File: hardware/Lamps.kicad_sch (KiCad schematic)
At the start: 3 parts

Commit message: 2/static version
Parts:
- removed C501: 100uF 10V, Capacitor_THT:CP_Radial_D6.3mm_P2.50mm, symbol Device:C_Polarized
- removed D501: ES1J, Diode_SMD:D_SMA_Handsoldering, symbol Device:D
- removed R501: 330R, Resistor_SMD:R_0603_1608Metric, symbol Device:R
- added C401: 100uF 10V, Capacitor_THT:CP_Radial_D6.3mm_P2.50mm, symbol Device:C_Polarized
- added D401: ES1J, Diode_SMD:D_SMA, symbol Device:D
- added N401, N402, N403, N404: INS-1, mynixies:mynixies-INS-1, symbol mynixies:INS-1
- added Q401: MPSA42, Package_TO_SOT_THT:TO-92_Inline, symbol Transistor_BJT:MPSA42
- added R401, R402, R405, R407: 330K, Resistor_SMD:R_1206_3216Metric, symbol Device:R
- added R403: 10K, Resistor_SMD:R_0603_1608Metric, symbol Device:R
- added R404: 47K, Resistor_SMD:R_0603_1608Metric, symbol Device:R
- added R406: 330R, Resistor_SMD:R_0603_1608Metric, symbol Device:R
- added U401: 74HC595, Package_SO:TSSOP-16_4.4x5mm_P0.65mm, symbol 74xx:74HC595
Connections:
- net +5V: now also C401.2, D401.2 (A)
- net GND: now also C401.1, Q401.1 (E), R404.1, U401.13 (~{OE}), U401.8 (GND)
- new net: Q401.3 (C), R401.1, R402.1, R405.1, R407.1
- new net: N401.P$1 (C), R401.2
- new net: Q401.2 (B), R403.2, R404.2
- new net: N403.P$1 (C), R405.2
- new net: N404.P$1 (C), R407.2
- new net: N402.P$1 (C), R402.2
- new net +170V: N401.P$2 (A), N402.P$2 (A), N403.P$2 (A), N404.P$2 (A)
- new net +3V3: U401.10 (~{SRCLR}), U401.16 (VCC)
- new net COLONS: R403.1
- new net CS: U401.12 (RCLK)
- new net FIRST_SK6812MINI_VCC: D401.1 (K)
- new net SCK: U401.11 (SRCLK)
- new net SER: U401.14 (SER)
- new net SK6812MINI_DATA: R406.1
- new net ThreeDigits1/DIGIT_A: U401.15 (QA)
- new net ThreeDigits1/DIGIT_B: U401.1 (QB)
- new net ThreeDigits1/DIGIT_C: U401.2 (QC)
- new net ThreeDigits1/DIGIT_D: U401.3 (QD)
- new net ThreeDigits1/SK6812MINI_IN: R406.2
- new net ThreeDigits2/DIGIT_A: U401.4 (QE)
- new net ThreeDigits2/DIGIT_B: U401.5 (QF)
- new net ThreeDigits2/DIGIT_C: U401.6 (QG)
- new net ThreeDigits2/DIGIT_D: U401.7 (QH)
- no-connect marks 1 -> 2
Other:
- removed sheet Dots
- removed sheet TwoDigits1
- removed sheet TwoDigits2
- removed sheet TwoDigits3
- added sheet HighSideSwitch1 (HighSideSwitch.kicad_sch)
- added sheet HighSideSwitch2 (HighSideSwitch.kicad_sch)
- added sheet HighSideSwitch3 (HighSideSwitch.kicad_sch)
- added sheet ThreeDigits1 (ThreeDigits.kicad_sch)
- added sheet ThreeDigits2 (ThreeDigits.kicad_sch)

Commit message: Finalize schematics
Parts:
- N401, N402, N403, N404: footprint mynixies:mynixies-INS-1 -> NosLib:INS-1
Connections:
- net FIRST_SK6812MINI_VCC renamed ThreeDigits1/FIRST_SK6812MINI_VCC
- no-connect marks 2 -> 1
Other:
- moved on the sheet: C401, D401
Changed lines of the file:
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@@
 	)
 	(junction
-		(at 40.64 88.9)
+		(at 82.55 87.63)
 		(diameter 0)
 		(color 0 0 0 0)
@@
 	)
 	(junction
+		(at 96.52 87.63)
+		(diameter 0)
+		(color 0 0 0 0)
+	)
+	(junction
 		(at 128.27 81.28)
 		(diameter 0)
@@
 	)
 	(no_connect
-		(at 68.58 152.4)
-	)
-	(no_connect
 		(at 147.32 175.26)
 	)
@@
 	(wire
 		(pts
-			(xy 48.26 88.9) (xy 53.34 88.9)
+			(xy 90.17 87.63) (xy 96.52 87.63)
 		)
 		(stroke
@@
 	(wire
 		(pts
-			(xy 34.29 88.9) (xy 40.64 88.9)
+			(xy 76.2 87.63) (xy 82.55 87.63)
 		)
 		(stroke
@@
 	(wire
 		(pts
-			(xy 68.58 152.4) (xy 67.31 152.4)
-		)
-		(stroke
-			(width 0)
-			(type default)
-		)
-	)
-	(wire
-		(pts
 			(xy 128.27 81.28) (xy 152.4 81.28)
 		)
@@
 	(wire
 		(pts
+			(xy 96.52 87.63) (xy 121.92 87.63)
+		)
+		(stroke
+			(width 0)
+			(type default)
+		)
+	)
+	(wire
+		(pts
 			(xy 67.31 132.08) (xy 87.63 132.08)
 		)
@@
 		)
 	)
-	(label "FIRST_SK6812MINI_VCC"
-		(at 121.92 87.63 180)
-		(effects
-			(font
-				(size 1.27 1.27)
-			)
-			(justify right bottom)
-		)
-	)
-	(label "FIRST_SK6812MINI_VCC"
-		(at 53.34 88.9 0)
-		(effects
-			(font
-				(size 1.27 1.27)
-			)
-			(justify left bottom)
-		)
-	)
 	(hierarchical_label "+3V3"
 		(shape input)
@@
 	(hierarchical_label "+5V"
 		(shape input)
-		(at 34.29 88.9 180)
+		(at 76.2 87.63 180)
 		(effects
 			(font
@@
 	)
 	(symbol
+		(lib_id "power:PWR_FLAG")
+		(at 96.52 87.63 0)
+		(unit 1)
+		(exclude_from_sim no)
+		(in_bom yes)
+		(on_board yes)
+		(dnp no)
+		(fields_autoplaced yes)
+		(property "Reference" "#FLG0401"
+			(at 96.52 85.725 0)
+			(effects
+				(font
+					(size 1.27 1.27)
+				)
+				(hide yes)
+			)
+		)
+		(property "Value" "PWR_FLAG"
+			(at 96.52 82.55 0)
+			(effects
+				(font
+					(size 1.27 1.27)
+				)
+			)
+		)
+		(property "Footprint" ""
+			(at 96.52 87.63 0)
+			(effects
+				(font
+					(size 1.27 1.27)
+				)
+				(hide yes)
+			)
+		)
+		(property "Datasheet" "~"
+			(at 96.52 87.63 0)
+			(effects
+				(font
+					(size 1.27 1.27)
+				)
+				(hide yes)
+			)
+		)
+		(property "Description" "Special symbol for telling ERC where power comes from"
+			(at 96.52 87.63 0)
+			(effects
+				(font
+					(size 1.27 1.27)
+				)
+				(hide yes)
+			)
+		)
+		(pin "1"
+		)
+		(instances
+			(project "NosClock"
+				(path "/5a46aee9-b968-477e-a4a1-4edba06163a3/cbfce168-24b0-4ff9-a45f-71f9f499ca5c"
+					(reference "#FLG0401")
+					(unit 1)
+				)
+			)
+		)
+	)
+	(symbol
 		(lib_id "Device:R")
 		(at 240.03 40.64 90)
@@
 	(symbol
 		(lib_id "Device:D")
-		(at 44.45 88.9 180)
+		(at 86.36 87.63 180)
 		(unit 1)
 		(exclude_from_sim no)
@@
 		(fields_autoplaced yes)
 		(property "Reference" "D401"
-			(at 44.45 82.55 0)
+			(at 86.36 81.28 0)
 			(effects
 				(font
@@
 		)
 		(property "Value" "ES1J"
-			(at 44.45 85.09 0)
+			(at 86.36 83.82 0)
 			(effects
 				(font
@@
 		)
 		(property "Footprint" "Diode_SMD:D_SMA"
-			(at 44.45 88.9 0)
+			(at 86.36 87.63 0)
 			(effects
 				(font
@@
 		)
 		(property "Datasheet" "~"
-			(at 44.45 88.9 0)
+			(at 86.36 87.63 0)
 			(effects
 				(font
@@
 		)
 		(property "Description" "Diode"
-			(at 44.45 88.9 0)
+			(at 86.36 87.63 0)
 			(effects
 				(font
@@
 		)
 		(property "Sim.Device" "D"
-			(at 44.45 88.9 0)
+			(at 86.36 87.63 0)
 			(effects
 				(font
@@
 		)
 		(property "Sim.Pins" "1=K 2=A"
-			(at 44.45 88.9 0)
+			(at 86.36 87.63 0)
 			(effects
 				(font
@@
 		)
 		(property "Availability" ""
-			(at 44.45 88.9 0)
+			(at 86.36 87.63 0)
 			(effects
 				(font
@@
 		)
 		(property "Check_prices" ""
-			(at 44.45 88.9 0)
+			(at 86.36 87.63 0)
 			(effects
 				(font
@@
 		)
 		(property "Description_1" ""
-			(at 44.45 88.9 0)
+			(at 86.36 87.63 0)
 			(effects
 				(font
@@
 		)
 		(property "MF" ""
-			(at 44.45 88.9 0)
+			(at 86.36 87.63 0)
 			(effects
 				(font
@@
 		)
 		(property "MP" ""
-			(at 44.45 88.9 0)
+			(at 86.36 87.63 0)
 			(effects
 				(font
@@
 		)
 		(property "PARTNO" ""
-			(at 44.45 88.9 0)
+			(at 86.36 87.63 0)
 			(effects
 				(font
@@
 		)
 		(property "Package" ""
-			(at 44.45 88.9 0)
+			(at 86.36 87.63 0)
 			(effects
 				(font
@@
 		)
 		(property "Price" ""
-			(at 44.45 88.9 0)
+			(at 86.36 87.63 0)
 			(effects
 				(font
@@
 		)
 		(property "SnapEDA_Link" ""
-			(at 44.45 88.9 0)
+			(at 86.36 87.63 0)
 			(effects
 				(font
@@
 			)
 		)
-		(property "Footprint" "mynixies:mynixies-INS-1"
+		(property "Footprint" "NosLib:INS-1"
 			(at 252.222 101.6 0)
 			(effects
@@
 	(symbol
 		(lib_id "power:GND")
-		(at 40.64 96.52 0)
+		(at 82.55 95.25 0)
 		(unit 1)
 		(exclude_from_sim no)
@@
 		(fields_autoplaced yes)
 		(property "Reference" "#PWR0401"
-			(at 40.64 102.87 0)
+			(at 82.55 101.6 0)
 			(effects
 				(font
@@
 		)
 		(property "Value" "GND"
-			(at 40.64 101.6 0)
+			(at 82.55 100.33 0)
 			(effects
 				(font
@@
 		)
 		(property "Footprint" ""
-			(at 40.64 96.52 0)
+			(at 82.55 95.25 0)
 			(effects
 				(font
@@
 		)
 		(property "Datasheet" ""
-			(at 40.64 96.52 0)
+			(at 82.55 95.25 0)
 			(effects
 				(font
@@
 		)
 		(property "Description" "Power symbol creates a global label with name \"GND\" , ground"
-			(at 40.64 96.52 0)
+			(at 82.55 95.25 0)
 			(effects
 				(font
@@
 	(symbol
 		(lib_id "Device:C_Polarized")
-		(at 40.64 92.71 180)
+		(at 82.55 91.44 180)
 		(unit 1)
 		(exclude_from_sim no)
@@
 		(fields_autoplaced yes)
 		(property "Reference" "C401"
-			(at 44.45 92.3289 0)
+			(at 86.36 91.0589 0)
 			(effects
 				(font
@@
 		)
 		(property "Value" "100uF 10V"
-			(at 44.45 94.8689 0)
+			(at 86.36 93.5989 0)
 			(effects
 				(font
@@
 		)
 		(property "Footprint" "Capacitor_THT:CP_Radial_D6.3mm_P2.50mm"
-			(at 39.6748 88.9 0)
+			(at 81.5848 87.63 0)
 			(effects
 				(font
@@
 		)
 		(property "Datasheet" "~"
-			(at 40.64 92.71 0)
+			(at 82.55 91.44 0)
 			(effects
 				(font
@@
 		)
 		(property "Description" "Polarized capacitor"
-			(at 40.64 92.71 0)
+			(at 82.55 91.44 0)
 			(effects
 				(font
@@
 			)
 		)
-		(property "Footprint" "mynixies:mynixies-INS-1"
+		(property "Footprint" "NosLib:INS-1"
 			(at 252.222 128.27 0)
 			(effects
@@
 			)
 		)
-		(property "Footprint" "mynixies:mynixies-INS-1"
+		(property "Footprint" "NosLib:INS-1"
 			(at 252.222 36.83 0)
 			(effects
@@
 			)
 		)
-		(property "Footprint" "mynixies:mynixies-INS-1"
+		(property "Footprint" "NosLib:INS-1"
 			(at 252.222 63.5 0)
 			(effects

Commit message: Fixes
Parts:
- removed Q401: MPSA42, Package_TO_SOT_THT:TO-92_Inline, symbol Transistor_BJT:MPSA42
- added Q402: MMBTA42, Package_TO_SOT_SMD:SOT-23, symbol Transistor_BJT:MMBTA42
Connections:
- net GND: now also Q402.2 (E)
- net at R401.1, R402.1, R405.1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: now also Q402.3 (C)
- net at R403.2, R404.2: now also Q402.1 (B)
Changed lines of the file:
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@@
-	)
-	(symbol
-		(lib_id "Transistor_BJT:MPSA42")
-		(at 214.63 95.25 0)
-		(unit 1)
-		(exclude_from_sim no)
-		(in_bom yes)
-		(on_board yes)
-		(dnp no)
-		(fields_autoplaced yes)
-		(property "Reference" "Q401"
-			(at 219.71 93.9799 0)
-			(effects
-				(font
-					(size 1.27 1.27)
-				)
-				(justify left)
-			)
-		)
-		(property "Value" "MPSA42"
-			(at 219.71 96.5199 0)
-			(effects
-				(font
-					(size 1.27 1.27)
-				)
-				(justify left)
-			)
-		)
-		(property "Footprint" "Package_TO_SOT_THT:TO-92_Inline"
-			(at 219.71 97.155 0)
-			(effects
-				(font
-					(size 1.27 1.27)
-					(italic yes)
-				)
-				(justify left)
-				(hide yes)
-			)
-		)
-		(property "Datasheet" "http://www.onsemi.com/pub_link/Collateral/MPSA42-D.PDF"
-			(at 214.63 95.25 0)
-			(effects
-				(font
-					(size 1.27 1.27)
-				)
-				(justify left)
-				(hide yes)
-			)
-		)
-		(property "Description" "0.5A Ic, 300V Vce, NPN High Voltage Transistor, TO-92"
-			(at 214.63 95.25 0)
-			(effects
-				(font
-					(size 1.27 1.27)
-				)
-				(hide yes)
-			)
-		)
-		(pin "2"
-		)
-		(pin "3"
-		)
-		(pin "1"
-		)
-		(instances
-			(project "NosClock"
-				(path "/5a46aee9-b968-477e-a4a1-4edba06163a3/cbfce168-24b0-4ff9-a45f-71f9f499ca5c"
-					(reference "Q401")
-					(unit 1)
-				)
-			)
-		)
 	)
 	(symbol
@@
 					(unit 1)
 				)
+			)
+		)
+	)
+	(symbol
+		(lib_id "Transistor_BJT:MMBTA42")
+		(at 214.63 95.25 0)
+		(unit 1)
+		(exclude_from_sim no)
+		(in_bom yes)
+		(on_board yes)
+		(dnp no)
+		(fields_autoplaced yes)
+		(property "Reference" "Q402"
+			(at 219.71 93.9799 0)
+			(effects
+				(font
+					(size 1.27 1.27)
+				)
+				(justify left)
+			)
+		)
+		(property "Value" "MMBTA42"
+			(at 219.71 96.5199 0)
+			(effects
+				(font
+					(size 1.27 1.27)
+				)
+				(justify left)
+			)
+		)
+		(property "Footprint" "Package_TO_SOT_SMD:SOT-23"
+			(at 219.71 97.155 0)
+			(effects
+				(font
+					(size 1.27 1.27)
+					(italic yes)
+				)
+				(justify left)
+				(hide yes)
+			)
+		)
+		(property "Datasheet" "https://www.onsemi.com/pub/Collateral/MMBTA42LT1-D.PDF"
+			(at 214.63 95.25 0)
+			(effects
+				(font
+					(size 1.27 1.27)
+				)
+				(justify left)
+				(hide yes)
+			)
+		)
+		(property "Description" "0.5A Ic, 300V Vce, NPN High Voltage Transistor, SOT-23"
+			(at 214.63 95.25 0)
+			(effects
+				(font
+					(size 1.27 1.27)
+				)
+				(hide yes)
+			)
+		)
+		(pin "3"
+		)
+		(pin "1"
+		)
+		(pin "2"
+		)
+		(instances
+			(project "NosClock"
+				(path "/5a46aee9-b968-477e-a4a1-4edba06163a3/cbfce168-24b0-4ff9-a45f-71f9f499ca5c"
+					(reference "Q402")
+					(unit 1)
+				)

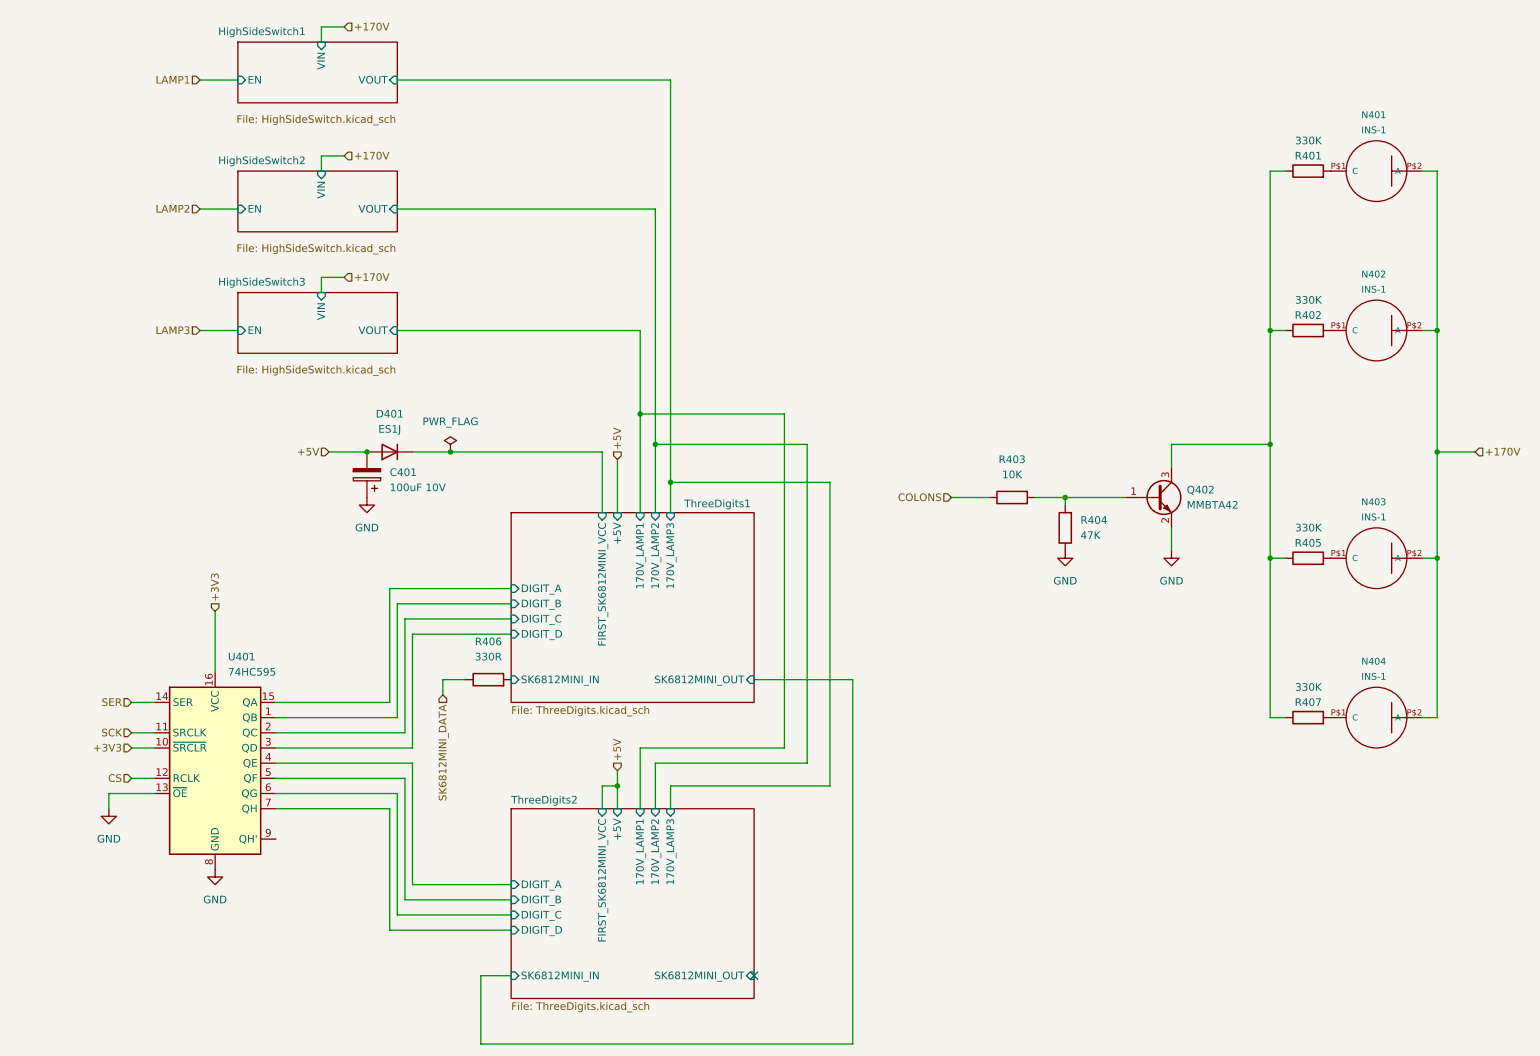
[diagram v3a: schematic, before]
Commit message: Lamps tracing
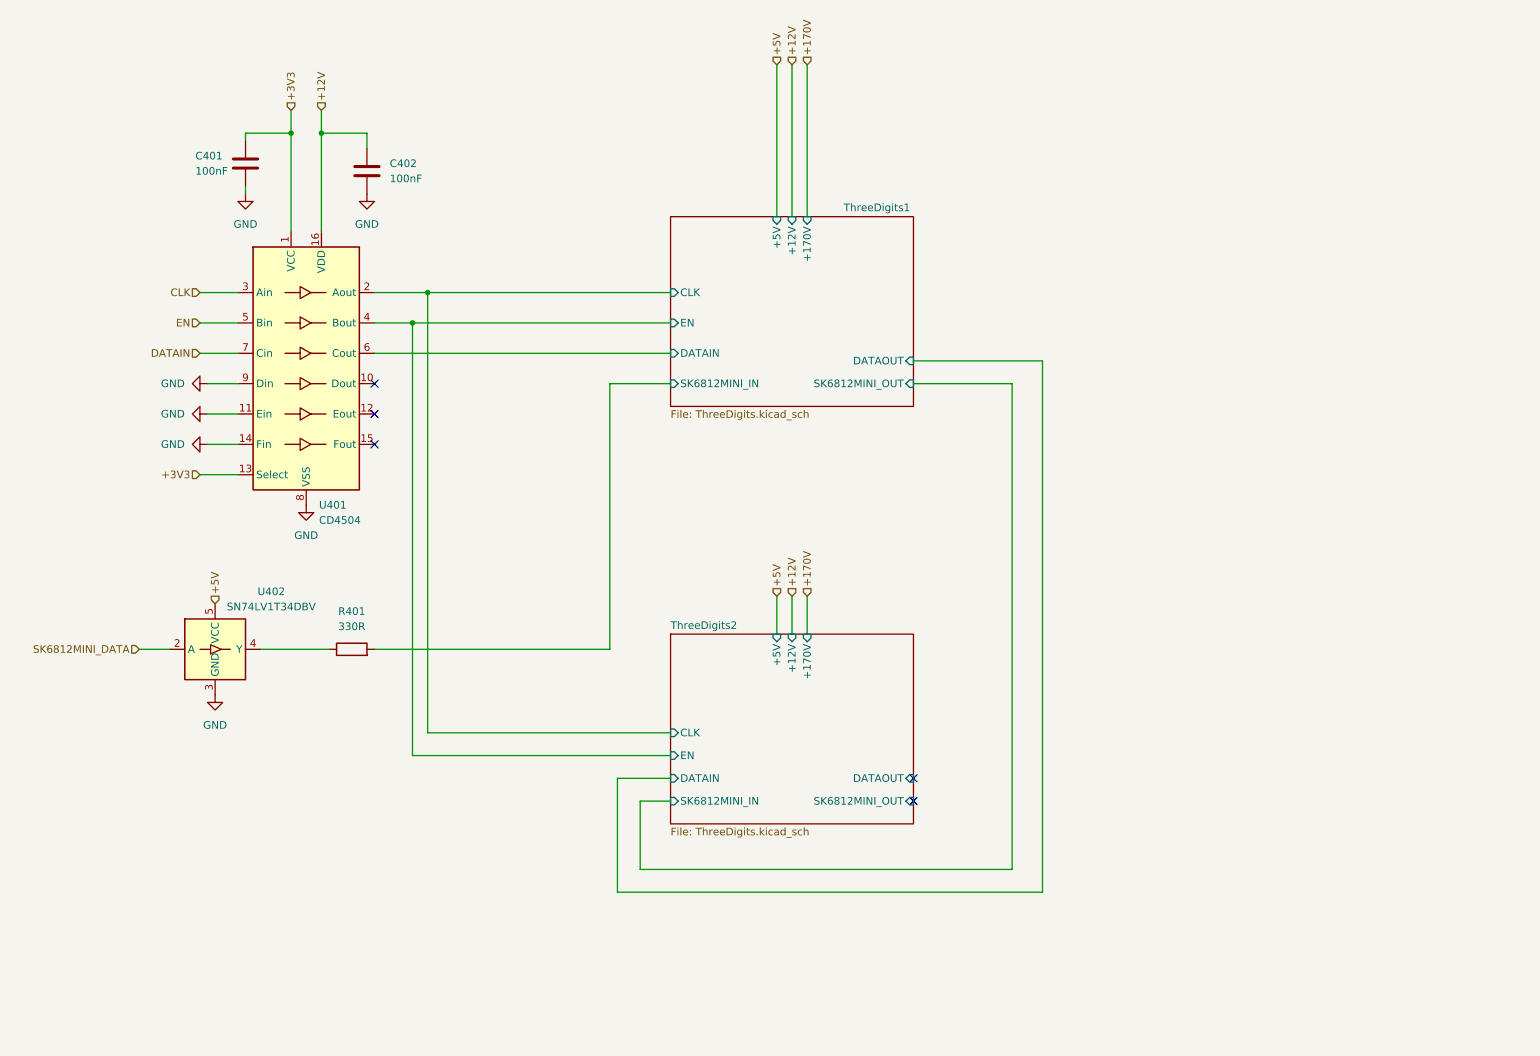
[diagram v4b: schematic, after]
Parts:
- removed C401: 100uF 10V, Capacitor_THT:CP_Radial_D6.3mm_P2.50mm, symbol Device:C_Polarized
- removed D401: ES1J, Diode_SMD:D_SMA, symbol Device:D
- removed N401, N402, N403, N404: INS-1, NosLib:INS-1, symbol mynixies:INS-1
- removed Q402: MMBTA42, Package_TO_SOT_SMD:SOT-23, symbol Transistor_BJT:MMBTA42
- removed R402, R405, R407: 330K, Resistor_SMD:R_1206_3216Metric, symbol Device:R
- removed R403: 10K, Resistor_SMD:R_0603_1608Metric, symbol Device:R
- removed R404: 47K, Resistor_SMD:R_0603_1608Metric, symbol Device:R
- removed R406: 330R, Resistor_SMD:R_0603_1608Metric, symbol Device:R
- removed U401: 74HC595, Package_SO:TSSOP-16_4.4x5mm_P0.65mm, symbol 74xx:74HC595
- added C401, C402: 100nF, Capacitor_SMD:C_0603_1608Metric, symbol Device:C
- added U401: CD4504, Package_SO:TSSOP-16_4.4x5mm_P0.65mm, symbol 4xxx:4504
- added U402: SN74LV1T34DBV, Package_TO_SOT_SMD:SOT-23-5, symbol Logic_LevelTranslator:SN74LV1T34DBV
- R401: value 330K -> 330R; footprint Resistor_SMD:R_1206_3216Metric -> Resistor_SMD:R_0603_1608Metric
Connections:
- net +3V3: now also C401.1, U401.1 (VCC), U401.13 (Select)
- net +5V: now also U402.5 (VCC)
- net GND: now also C401.2, C402.2, U401.11 (Ein), U401.14 (Fin), U401.8 (VSS), U401.9 (Din), U402.3 (GND)
- net SK6812MINI_DATA: now also U402.2 (A)
- net ThreeDigits1/SK6812MINI_IN: now also R401.2
- net at R401.1: now also U402.4 (Y)
- new net +12V: C402.1, U401.16 (VDD)
- new net CLK: U401.3 (Ain)
- new net DATAIN: U401.7 (Cin)
- new net EN: U401.5 (Bin)
- new net ThreeDigits1/CLK: U401.2 (Aout)
- new net ThreeDigits1/DATAIN: U401.6 (Cout)
- new net ThreeDigits1/EN: U401.4 (Bout)
- no-connect marks 1 -> 5
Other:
- removed sheet HighSideSwitch1
- removed sheet HighSideSwitch2
- removed sheet HighSideSwitch3
- sheet ThreeDigits1 ports: added +12V, +170V, CLK, DATAIN, DATAOUT, EN; removed 170V_LAMP1, 170V_LAMP2, 170V_LAMP3, DIGIT_A, DIGIT_B, DIGIT_C, DIGIT_D, FIRST_SK6812MINI_VCC
- sheet ThreeDigits2 ports: added +12V, +170V, CLK, DATAIN, DATAOUT, EN; removed 170V_LAMP1, 170V_LAMP2, 170V_LAMP3, DIGIT_A, DIGIT_B, DIGIT_C, DIGIT_D, FIRST_SK6812MINI_VCC
